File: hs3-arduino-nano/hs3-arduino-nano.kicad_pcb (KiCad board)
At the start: 2 copper layers, 17.8 x 43.2 mm, 40 parts, among them J1 PWR, J2 USB_B_Micro, J3 DEBUG, J4 I2C, J5 Sensors, J6 ADC, J7 3V3, J8 GND, P3 CONN_01X01, P4 CONN_01X01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

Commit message: Minor cleanup in element placement
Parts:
- moved J4 14.1 mm to (140.1, 86.0), turned to -90 degrees
- moved J5 1.88 mm to (140.1, 93.9), turned to -90 degrees
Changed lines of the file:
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@@
       (effects (font (size 1 1) (thickness 0.15)))
     )
-    (fp_text value "Bootsel" (at 0.889 1.555) (layer "B.SilkS")
+    (fp_text value "Bootsel" (at 0.254 1.682) (layer "B.SilkS")
       (effects (font (size 1 1) (thickness 0.15)) (justify mirror))
     )
@@
       (effects (font (size 1 1) (thickness 0.15)))
     )
-    (fp_text value "ADC" (at -1.27 4.435 90) (layer "B.SilkS")
+    (fp_text value "ADC" (at 1.778 3.8 90) (layer "B.SilkS")
       (effects (font (size 1 1) (thickness 0.15)) (justify mirror))
     )
@@
   )
   (footprint "Connector_Hirose:Hirose_DF13-04P-1.25DSA_1x04_P1.25mm_Vertical" (layer "F.Cu")
-    (at 141.097 100.076 90)
+    (at 140.081 85.979 -90)
     (descr "Hirose DF13 through hole, DF13-04P-1.25DSA, 4 Pins per row (https://www.hirose.com/product/en/products/DF13/DF13-2P-1.25DSA%2850%29/), generated with kicad-footprint-generator")
     (tags "connector Hirose DF13 vertical")
@@
     (fp_line (start -0.5 1.2) (end 0 0.492893) (layer "F.Fab") (width 0.1))
     (fp_line (start 5.2 -2.2) (end -1.45 -2.2) (layer "F.Fab") (width 0.1))
-    (pad "1" thru_hole roundrect (at 0 0 90) (size 0.9 1.4) (drill 0.6) (layers *.Cu *.Mask) (roundrect_rratio 0.25)
+    (pad "1" thru_hole roundrect (at 0 0 270) (size 0.9 1.4) (drill 0.6) (layers *.Cu *.Mask) (roundrect_rratio 0.25)
       (net 14 "/GPIO0") (pinfunction "Pin_1") (pintype "passive"))
-    (pad "2" thru_hole oval (at 1.25 0 90) (size 0.9 1.4) (drill 0.6) (layers *.Cu *.Mask)
+    (pad "2" thru_hole oval (at 1.25 0 270) (size 0.9 1.4) (drill 0.6) (layers *.Cu *.Mask)
       (net 15 "/GPIO1") (pinfunction "Pin_2") (pintype "passive"))
-    (pad "3" thru_hole oval (at 2.5 0 90) (size 0.9 1.4) (drill 0.6) (layers *.Cu *.Mask)
+    (pad "3" thru_hole oval (at 2.5 0 270) (size 0.9 1.4) (drill 0.6) (layers *.Cu *.Mask)
       (net 16 "/GPIO2") (pinfunction "Pin_3") (pintype "passive"))
-    (pad "4" thru_hole oval (at 3.75 0 90) (size 0.9 1.4) (drill 0.6) (layers *.Cu *.Mask)
+    (pad "4" thru_hole oval (at 3.75 0 270) (size 0.9 1.4) (drill 0.6) (layers *.Cu *.Mask)
       (net 17 "/GPIO3") (pinfunction "Pin_4") (pintype "passive"))
     (model "${KICAD6_3DMODEL_DIR}/Connector_Hirose.3dshapes/Hirose_DF13-04P-1.25DSA_1x04_P1.25mm_Vertical.wrl"
@@
       (effects (font (size 1 1) (thickness 0.15)))
     )
-    (fp_text value "DEBUG" (at -1.778 1.275 180) (layer "B.SilkS")
+    (fp_text value "DEBUG" (at -1.778 1.148 180) (layer "B.SilkS")
       (effects (font (size 1 1) (thickness 0.15)) (justify mirror))
     )
@@
   )
   (footprint "Connector_Hirose:Hirose_DF13-06P-1.25DSA_1x06_P1.25mm_Vertical" (layer "F.Cu")
-    (at 140.97 92.202 90)
+    (at 140.081 93.853 -90)
     (descr "Hirose DF13 through hole, DF13-06P-1.25DSA, 6 Pins per row (https://www.hirose.com/product/en/products/DF13/DF13-2P-1.25DSA%2850%29/), generated with kicad-footprint-generator")
     (tags "connector Hirose DF13 vertical")
@@
     (fp_line (start 7.7 1.2) (end 7.7 -2.2) (layer "F.Fab") (width 0.1))
     (fp_line (start 7.7 -2.2) (end -1.45 -2.2) (layer "F.Fab") (width 0.1))
-    (pad "1" thru_hole roundrect (at 0 0 90) (size 0.9 1.4) (drill 0.6) (layers *.Cu *.Mask) (roundrect_rratio 0.25)
+    (pad "1" thru_hole roundrect (at 0 0 270) (size 0.9 1.4) (drill 0.6) (layers *.Cu *.Mask) (roundrect_rratio 0.25)
       (net 18 "/GPIO4") (pinfunction "Pin_1") (pintype "passive"))
-    (pad "2" thru_hole oval (at 1.25 0 90) (size 0.9 1.4) (drill 0.6) (layers *.Cu *.Mask)
+    (pad "2" thru_hole oval (at 1.25 0 270) (size 0.9 1.4) (drill 0.6) (layers *.Cu *.Mask)
       (net 19 "/GPIO5") (pinfunction "Pin_2") (pintype "passive"))
-    (pad "3" thru_hole oval (at 2.5 0 90) (size 0.9 1.4) (drill 0.6) (layers *.Cu *.Mask)
+    (pad "3" thru_hole oval (at 2.5 0 270) (size 0.9 1.4) (drill 0.6) (layers *.Cu *.Mask)
       (net 20 "/GPIO6") (pinfunction "Pin_3") (pintype "passive"))
-    (pad "4" thru_hole oval (at 3.75 0 90) (size 0.9 1.4) (drill 0.6) (layers *.Cu *.Mask)
+    (pad "4" thru_hole oval (at 3.75 0 270) (size 0.9 1.4) (drill 0.6) (layers *.Cu *.Mask)
       (net 21 "/GPIO7") (pinfunction "Pin_4") (pintype "passive"))
-    (pad "5" thru_hole oval (at 5 0 90) (size 0.9 1.4) (drill 0.6) (layers *.Cu *.Mask)
+    (pad "5" thru_hole oval (at 5 0 270) (size 0.9 1.4) (drill 0.6) (layers *.Cu *.Mask)
       (net 22 "/GPIO8") (pinfunction "Pin_5") (pintype "passive"))
-    (pad "6" thru_hole oval (at 6.25 0 90) (size 0.9 1.4) (drill 0.6) (layers *.Cu *.Mask)
+    (pad "6" thru_hole oval (at 6.25 0 270) (size 0.9 1.4) (drill 0.6) (layers *.Cu *.Mask)
       (net 23 "/GPIO9") (pinfunction "Pin_6") (pintype "passive"))
     (model "${KICAD6_3DMODEL_DIR}/Connector_Hirose.3dshapes/Hirose_DF13-06P-1.25DSA_1x06_P1.25mm_Vertical.wrl"

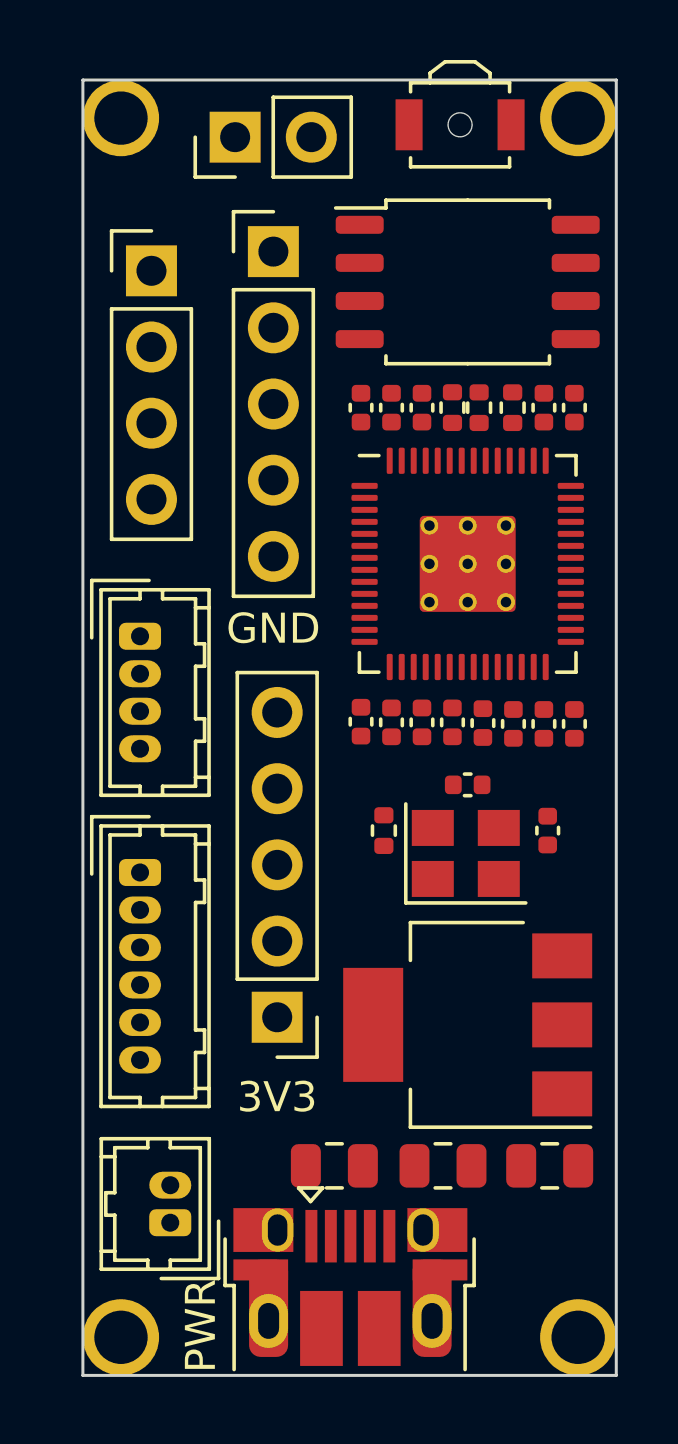
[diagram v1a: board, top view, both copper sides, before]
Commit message: First stab at routing
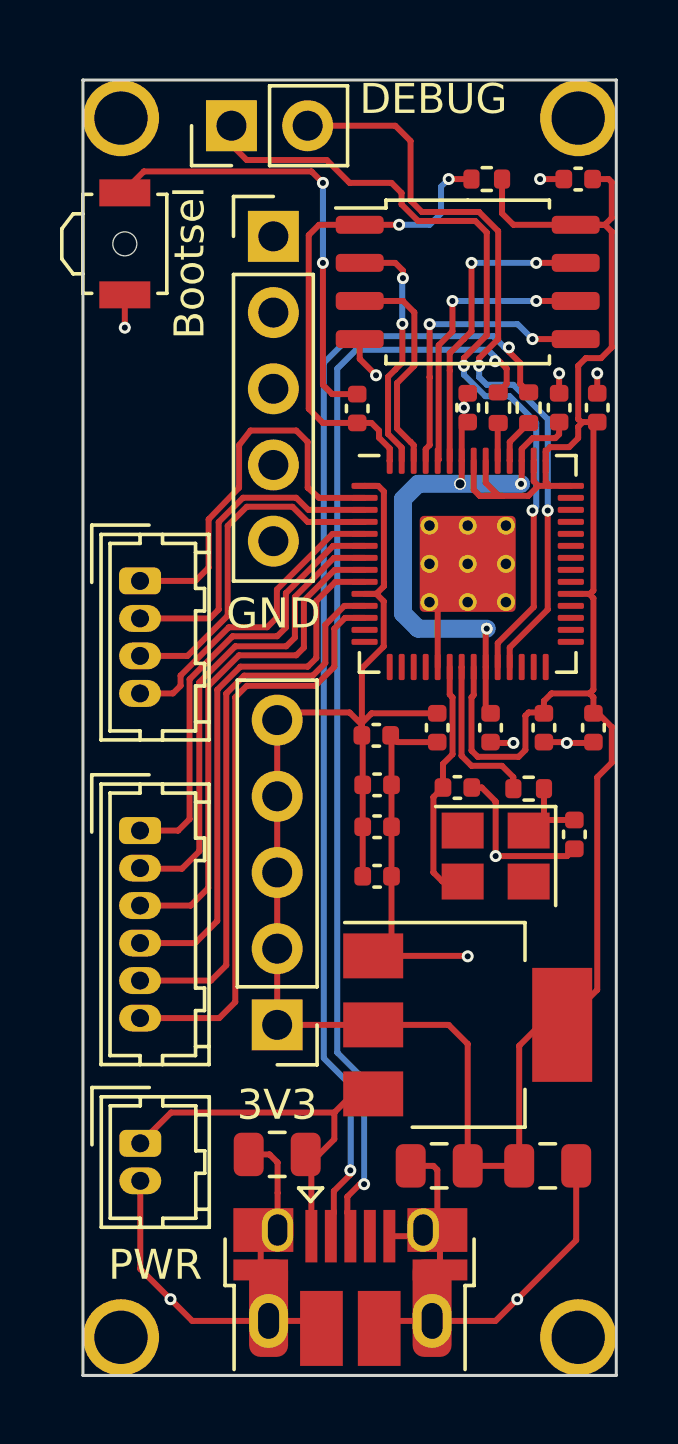
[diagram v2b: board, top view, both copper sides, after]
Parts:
- removed J6: ADC, Connector_PinHeader_2.54mm:PinHeader_1x04_P2.54mm_Vertical
- moved SW1 11.9 mm to (139.6, 72.9), turned to 90 degrees
- moved C4 9.84 mm to (154.7, 70.7), turned to 180 degrees
- moved R3 7.70 mm to (151.6, 70.7), turned to 180 degrees
- moved C13 5.34 mm to (148.0, 94.0), turned to 0 degrees
- moved R2 5.02 mm to (153.0, 91.1), turned to 0 degrees
- moved C2 3.92 mm to (154.6, 92.6), turned to -90 degrees
- moved C5 3.68 mm to (150.1, 103.6), turned to 180 degrees
- moved C12 3.51 mm to (148.0, 92.3), turned to 0 degrees
- moved C6 3.49 mm to (153.7, 103.6), turned to 0 degrees
- moved C1 3.34 mm to (150.7, 91.0), turned to 0 degrees
- moved J1 2.83 mm to (140.1, 102.9), turned to -90 degrees
- moved C8 2.80 mm to (151.8, 89.0)
- moved C16 2.67 mm to (155.2, 89.0)
- moved C14 2.58 mm to (148.0, 89.3), turned to 0 degrees
- moved C10 2.17 mm to (148.0, 90.9), turned to 0 degrees
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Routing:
- net +3V3: track 0.00 -> 107.0 mm
- net GND: track 0.00 -> 60.7 mm, vias 0 -> 12
- net /USB_D-: track 0.00 -> 38.2 mm, vias 0 -> 2
- net /USB_D+: track 0.00 -> 36.8 mm, vias 0 -> 2
- net /SWCLK: track 0.00 -> 27.4 mm, vias 0 -> 2
- net /SWD: track 0.00 -> 25.8 mm, vias 0 -> 2
- net /GPIO9: track 0.00 -> 19.7 mm
- net +1V1: track 0.00 -> 19.1 mm, vias 0 -> 3
- net /GPIO8: track 0.00 -> 18.7 mm
- net /GPIO7: track 0.00 -> 18.1 mm
- net /GPIO6: track 0.00 -> 17.0 mm
- net /QSPI_SS: track 0.00 -> 16.3 mm, vias 0 -> 2
- net /GPIO5: track 0.00 -> 15.9 mm
- net /~{USB_BOOT}: track 0.00 -> 15.4 mm, vias 0 -> 2
- net /GPIO4: track 0.00 -> 14.8 mm
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- added copper zone on B.Cu, net GND

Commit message: Redone placement, new routing
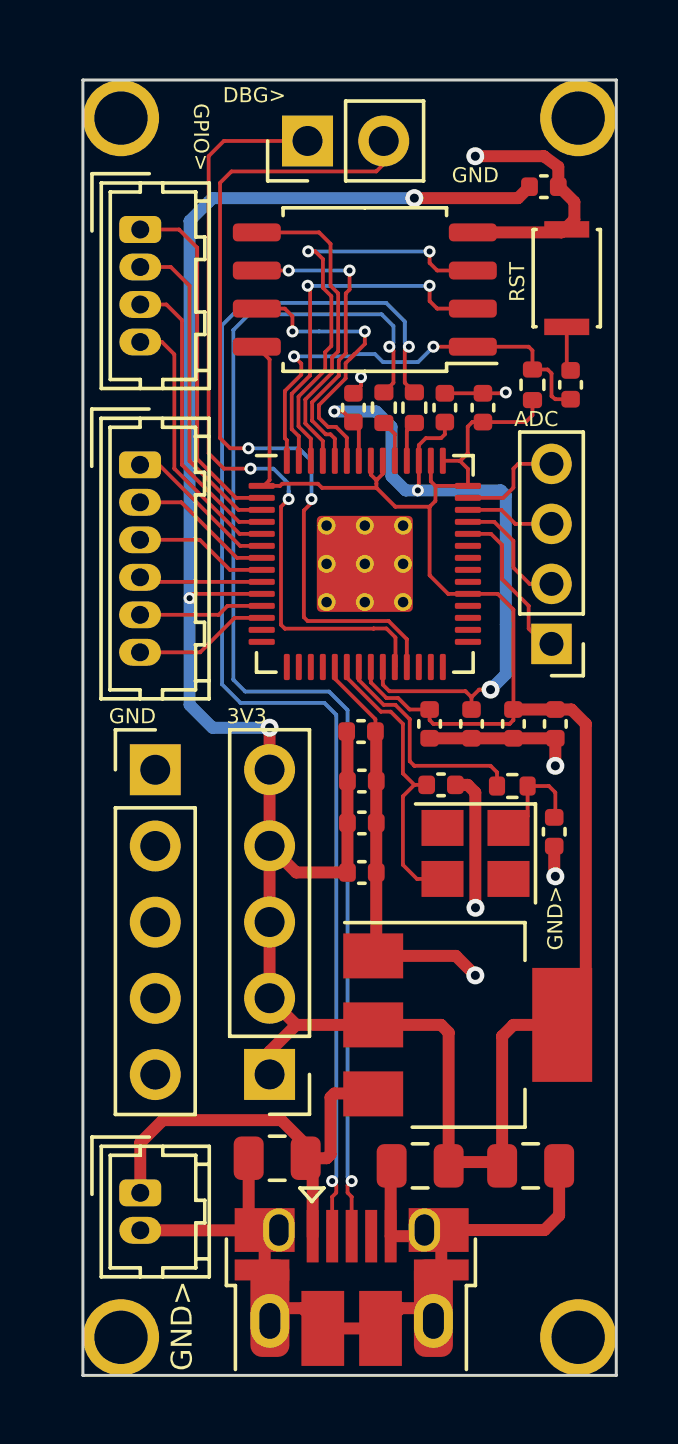
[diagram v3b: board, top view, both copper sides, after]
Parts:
- added ADC: Conn_01x04, Connector_PinHeader_2.00mm:PinHeader_1x04_P2.00mm_Vertical, F.Cu at (153.8, 86.2)
- J3: value DEBUG -> DBG
- SW1: value Bootsel -> Boot; footprint Button_Switch_SMD:SW_SPST_B3U-3000P-B -> Button_Switch_SMD:SW_SPST_CK_KXT3
- moved J8 18.2 mm to (140.6, 90.4)
- moved SW1 14.8 mm to (154.3, 74.0), turned to -90 degrees
- moved J5 12.2 mm to (140.1, 80.3)
- moved J4 11.7 mm to (140.1, 72.4)
- moved R1 7.16 mm to (154.4, 77.6)
- moved R3 7.03 mm to (153.2, 77.6), turned to 90 degrees
- moved G2 4.59 mm to (151.0, 96.8)
- moved C11 3.81 mm to (151.5, 78.4)
- moved R4 3.81 mm to (148.2, 78.4)
- moved R5 3.81 mm to (149.2, 78.4)
- moved C7 3.81 mm to (150.2, 78.4)
- moved C9 3.81 mm to (147.2, 78.4)
- moved U2 3.44 mm to (147.6, 74.4), turned to 180 degrees
- moved U3 3.43 mm to (147.6, 83.6)
- moved J3 2.59 mm to (145.7, 69.5)
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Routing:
- net /GPIO9: track 19.7 -> 4.53 mm
- net /GPIO8: track 18.7 -> 4.18 mm
- net /~{USB_BOOT}: track 15.4 -> 1.43 mm, vias 2 -> 0
- net /GPIO7: track 18.1 -> 4.12 mm
- net +3V3: track 107.0 -> 120.4 mm, vias 0 -> 3
- net /GPIO6: track 17.0 -> 4.47 mm
- net /GPIO5: track 15.9 -> 4.82 mm
- net /GPIO4: track 14.8 -> 5.17 mm
- net /QSPI_SD2: track 7.39 -> 14.0 mm, vias 0 -> 2
- net /GPIO26_ADC0: track 0.00 -> 6.29 mm
- net +1V1: track 19.1 -> 24.6 mm
- net /USB_D+: track 36.8 -> 41.8 mm
- net /USB_D-: track 38.2 -> 43.0 mm
- net /GPIO27_ADC1: track 0.00 -> 4.16 mm
- net /QSPI_SD1: track 8.28 -> 12.3 mm
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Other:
- board text added: "3V3"
- board text added: "ADC"
- board text added: "ADC0"
- board text added: "ADC1"
- board text added: "ADC2"
- board text added: "ADC3"
- board text added: "DBG>"
- board text added: "GND"
- board text added: "GND>"
- board text added: "GPIO>"
- board text added: "IO0"
- board text added: "IO1"
- board text added: "IO2"
- board text added: "IO3"
- board text added: "IO4"
- board text added: "IO5"
- board text added: "IO6"
- board text added: "IO7"
- board text added: "IO8"
- board text added: "IO9"
- board text added: "JLCJLCJLCJLC"
- board text added: "RST"
- board text added: "SWCLK"
- board text added: "SWD"
